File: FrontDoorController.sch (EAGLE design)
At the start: 2 parts

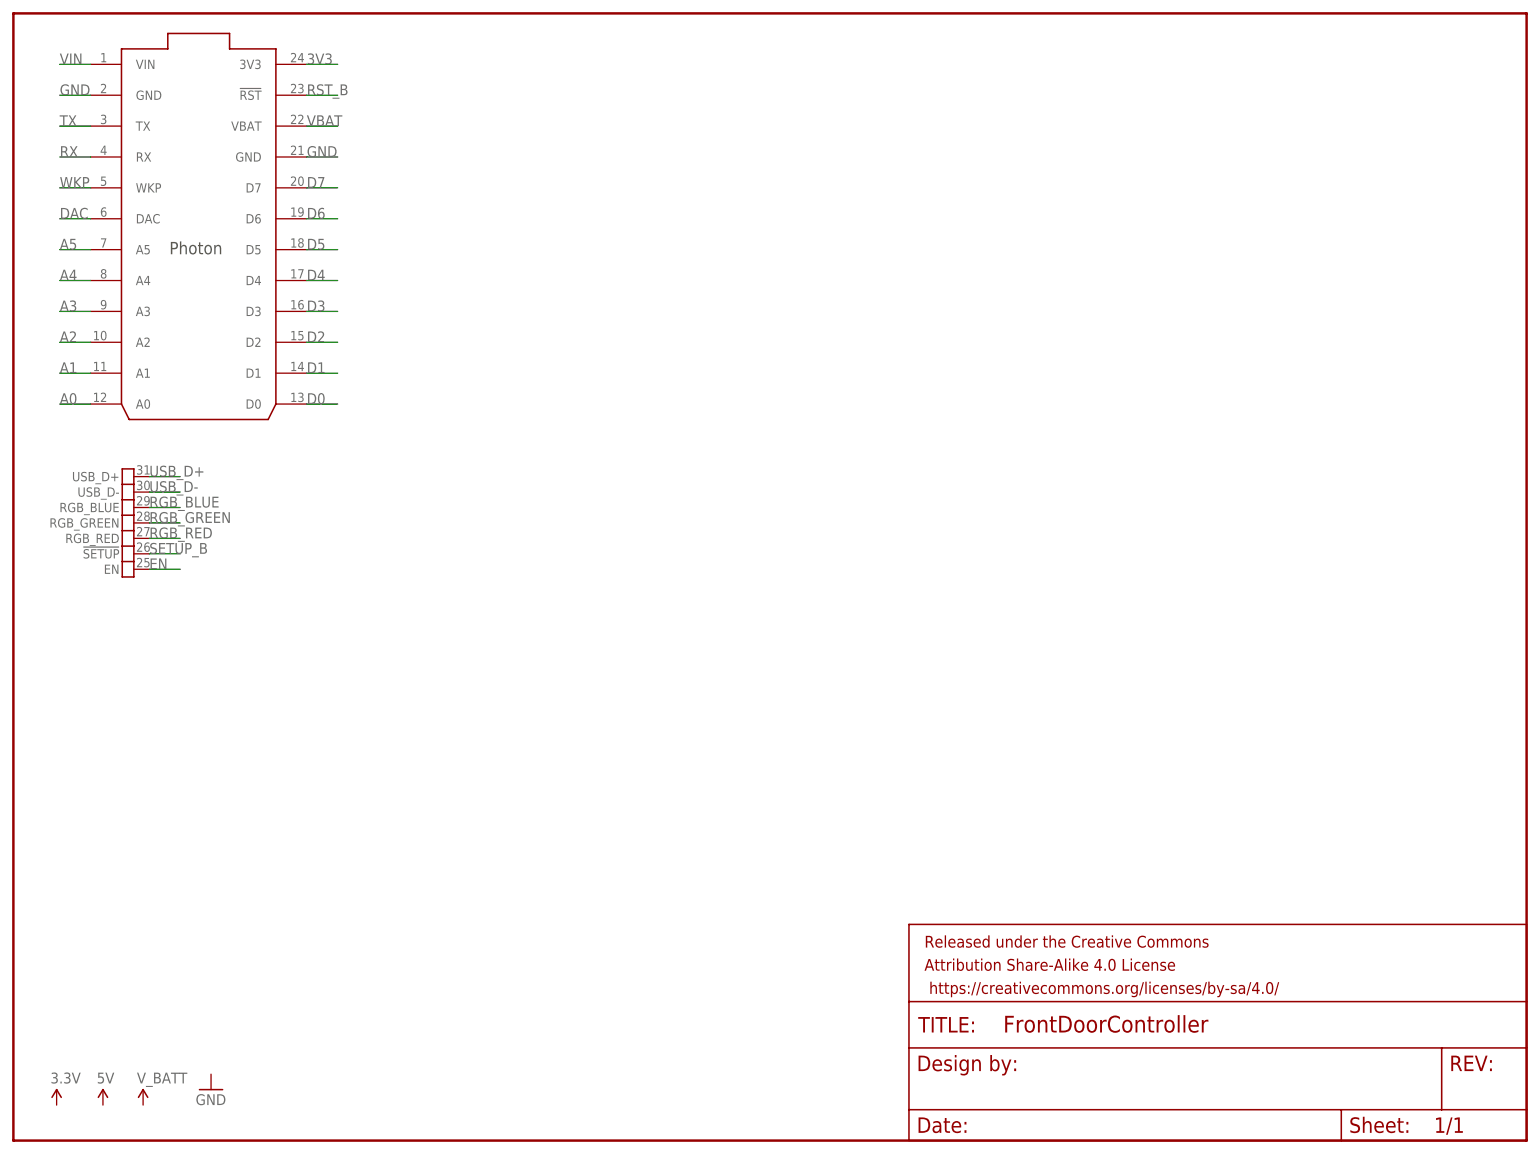
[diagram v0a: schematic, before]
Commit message: Door_Control_PCB: Add motor driver and connect
Add the TB6612FNG motor driver and connect it to the Photon.  This will
take power from 4 AA batteries in the Lockitron and drive the Lockitron
motor.  The Photon will control direction and speed for the motor.
Since there is only 1 motor on the Lockitron, only 1 of the input/output
pairs on the driver needs to be connected.
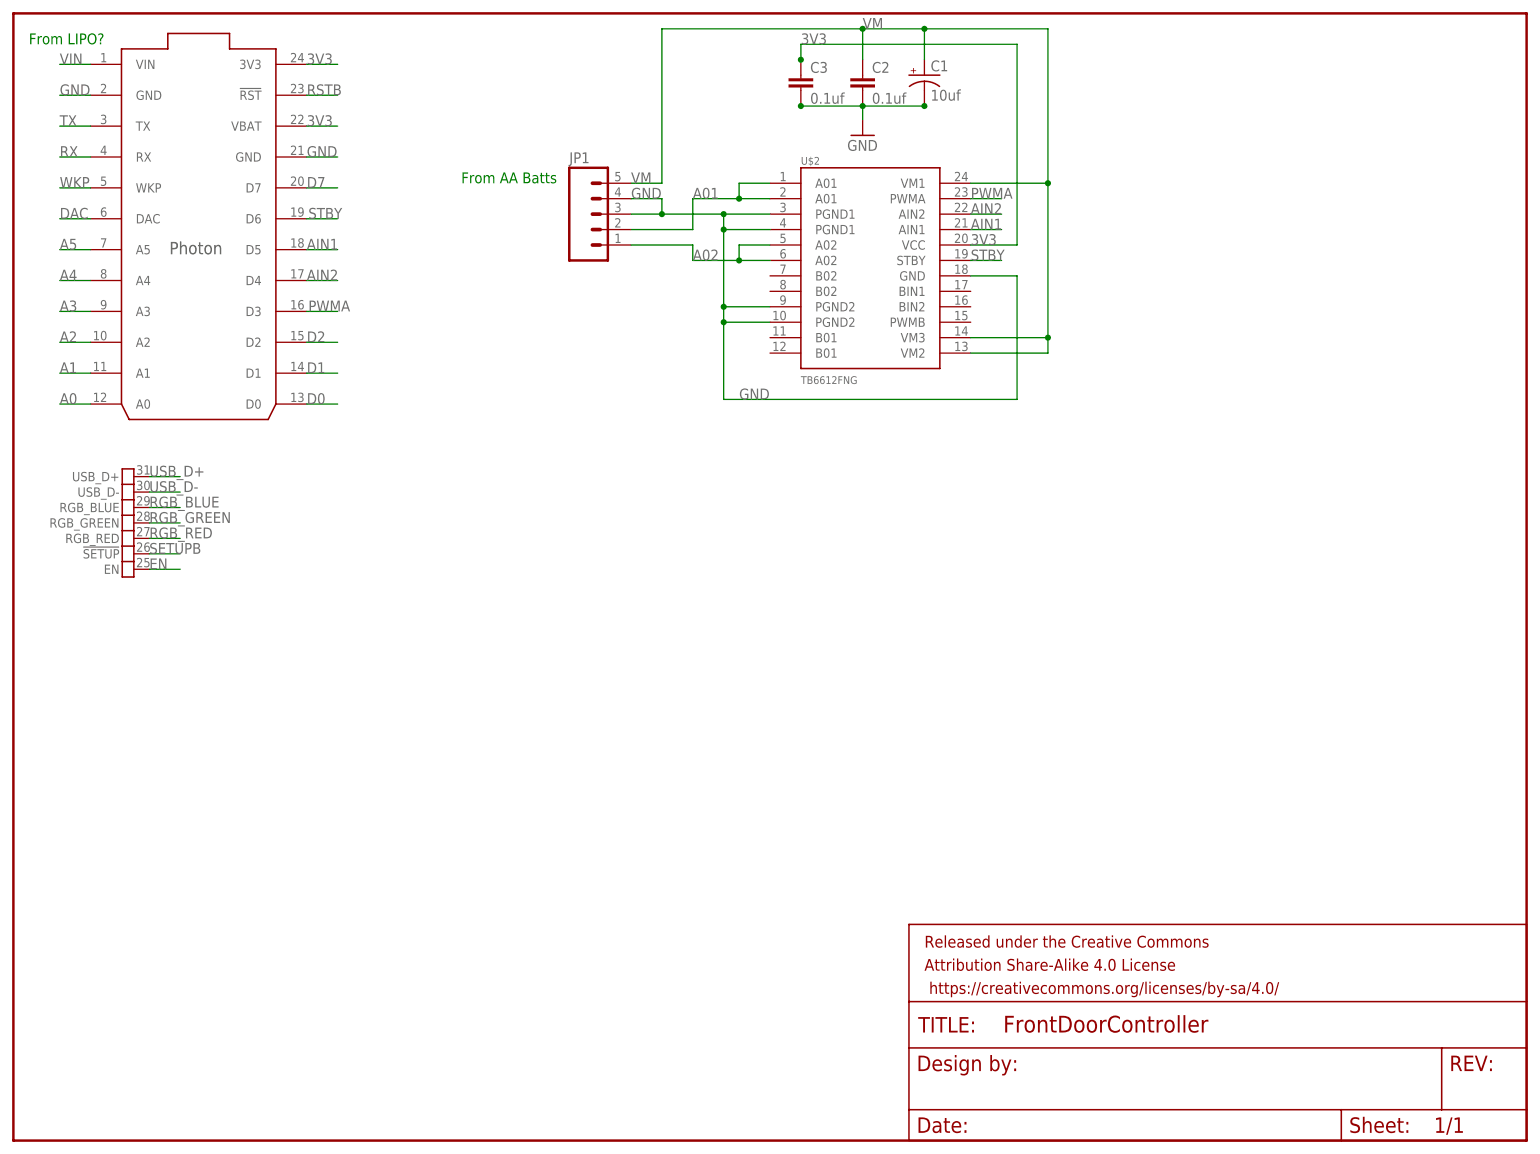
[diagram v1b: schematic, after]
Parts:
- added C1: 10uf, SparkFun-Capacitors:CAP_POL3528
- added C2, C3: 0.1uf, SparkFun-Capacitors:CAP0402-CAP
- added JP1: (no value), SparkFun-Connectors:M05SCREW
- added U$2: TB6612FNG, SparkFun-PowerIC:TB6612FNG
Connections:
- net RST_B renamed RSTB
- net SETUP_B renamed SETUPB
- removed net D3: U$1G$1.D3
- removed net D4: U$1G$1.D4
- removed net D5: U$1G$1.D5
- removed net D6: U$1G$1.D6
- removed net VBAT: U$1G$1.VBAT
- new net A01: JP1.2, U$2.A01@1, U$2.A01@2
- new net A02: JP1.1, U$2.A02@5, U$2.A02@6
- new net AIN1: U$1G$1.D5, U$2.AIN1
- new net AIN2: U$1G$1.D4, U$2.AIN2
- new net PWMA: U$1G$1.D3, U$2.PWMA
- new net STBY: U$1G$1.D6, U$2.STBY
- new net VM: C1.+, C2.1, JP1.5, U$2.VM1, U$2.VM2, U$2.VM3
- net 3V3: now also C3.1, U$1G$1.VBAT, U$2.VCC
- net GND: now also C1.-, C2.2, C3.2, JP1.3, JP1.4, U$2.GND, U$2.PGND1@3, U$2.PGND1@4, U$2.PGND2@10, U$2.PGND2@9
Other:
- note added: "From AA Batts"
- note added: "From LIPO?"

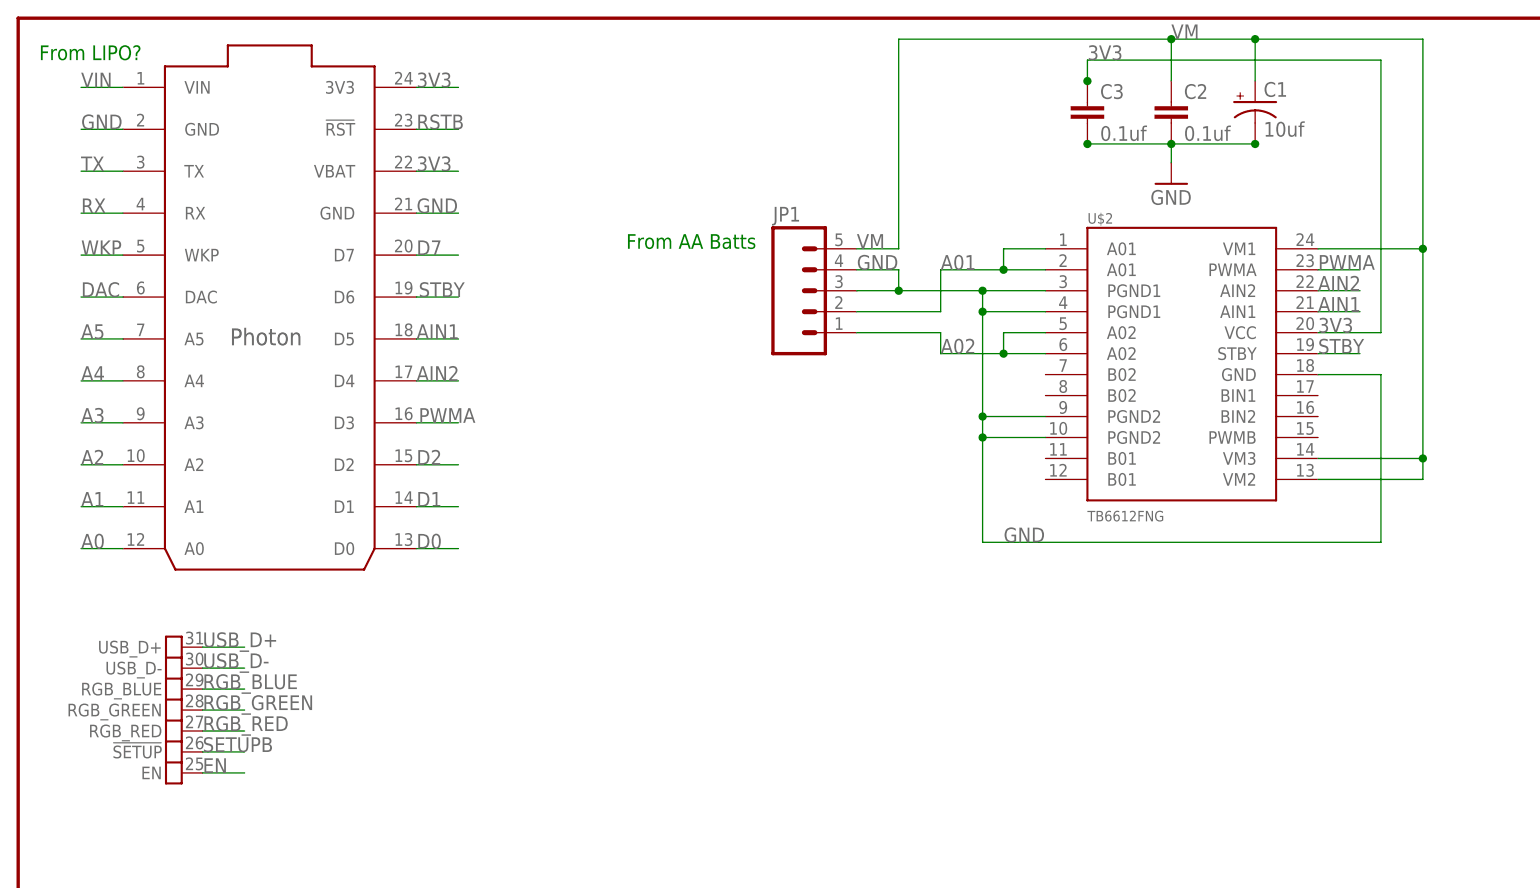
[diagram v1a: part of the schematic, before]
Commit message: Door_Control_PCB: Add headers and diode
Exchange the screw terminals for 0.1" breakaway header holes.  There is
no room for the screw terminals in the Lockitron so wires will need to
be soldered directly to the board.  Some space can be saved by using
0.1" spacing header holes instead of the bigger pitch screw terminals.
Also do a few other minor cleanup tasks like change the size of the wire
input labels.  Also add a 1N4001 diode between VM from AA's and VIN on
Photon to drop the voltage from about 6V to about 5V to ensure it is
safe for the Photon VIN input.
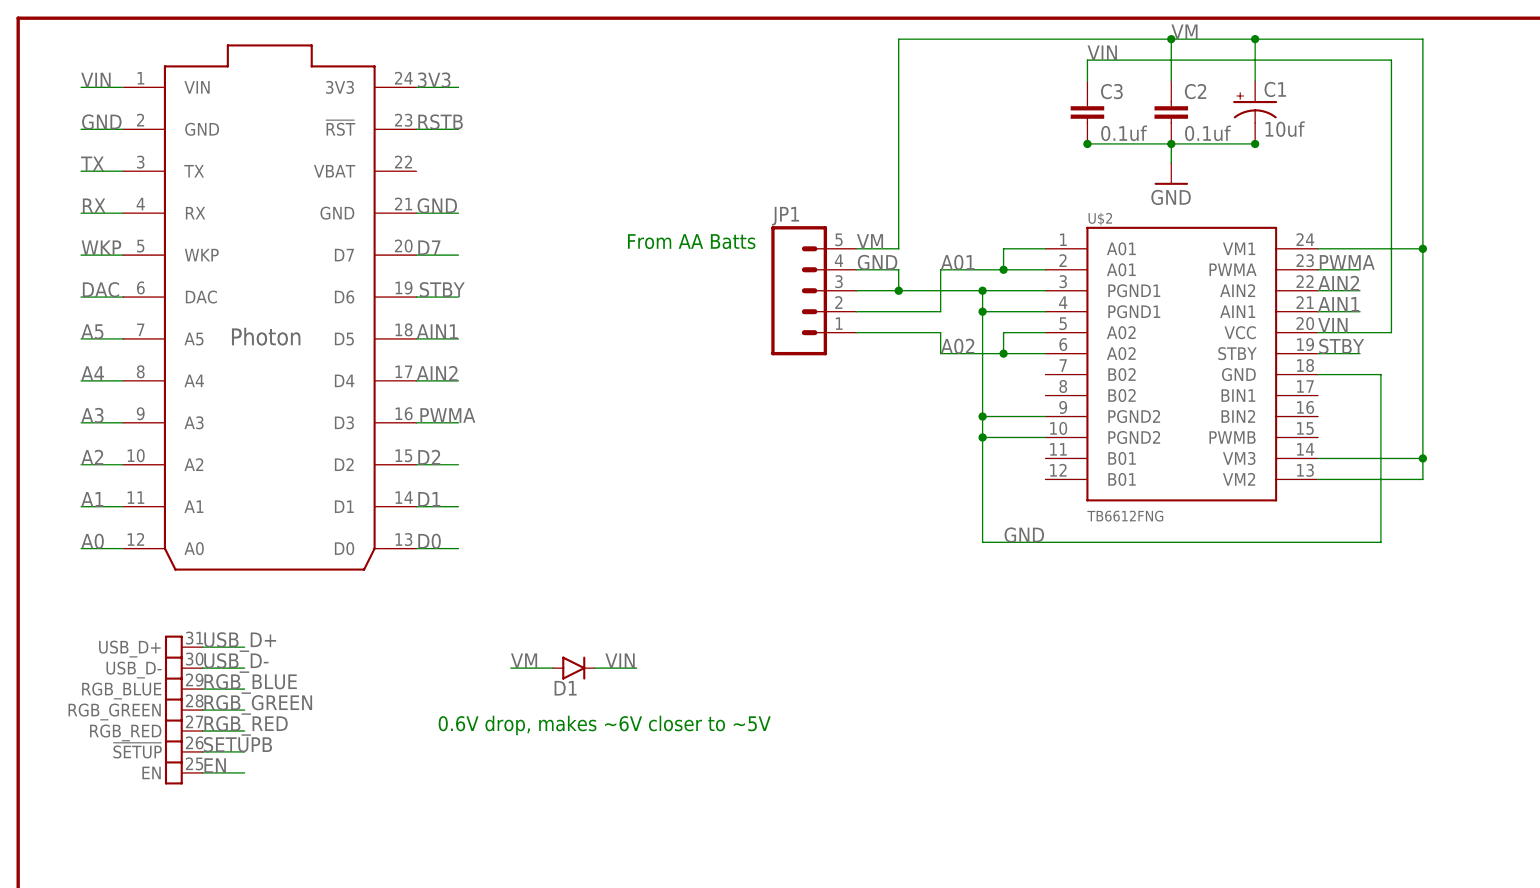
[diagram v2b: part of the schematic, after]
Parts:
- added D1: (no value), SparkFun-DiscreteSemi:DIODEPTH
- JP1: device SparkFun-Connectors:M05SCREW -> SparkFun-Connectors:M05PTH
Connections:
- net 3V3: no longer C3.1, U$1G$1.VBAT, U$2.VCC
- net VIN: now also C3.1, D1.C, U$2.VCC
- net VM: now also D1.A
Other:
- note added: "0.6V drop, makes ~6V closer to ~5V"
- note removed: "From LIPO?"
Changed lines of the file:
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@@
 <part name="C3" library="SparkFun-Capacitors" deviceset="CAP" device="0402-CAP" value="0.1uf"/>
 <part name="GND1" library="SparkFun-Aesthetics" deviceset="GND" device=""/>
-<part name="JP1" library="SparkFun-Connectors" deviceset="M05" device="SCREW"/>
+<part name="JP1" library="SparkFun-Connectors" deviceset="M05" device="PTH"/>
+<part name="D1" library="SparkFun-DiscreteSemi" deviceset="DIODE" device="PTH"/>
 </parts>
 <sheets>
@@
 <plain>
 <text x="73.66" y="157.48" size="1.778" layer="91">From AA Batts</text>
-<text x="2.54" y="180.34" size="1.778" layer="91">From LIPO?</text>
+<text x="50.8" y="99.06" size="1.778" layer="91">0.6V drop, makes ~6V closer to ~5V</text>
 </plain>
 <instances>
@@
 <instance part="GND1" gate="1" x="139.7" y="165.354"/>
 <instance part="JP1" gate="G$1" x="93.98" y="152.4"/>
+<instance part="D1" gate="G$1" x="67.31" y="106.68" smashed="yes">
+<attribute name="NAME" x="64.77" y="103.3526" size="1.778" layer="95"/>
+<attribute name="VALUE" x="69.85" y="104.3686" size="1.778" layer="96"/>
+</instance>
 </instances>
 <busses>
@@
 <wire x1="12.7" y1="177.038" x2="7.62" y2="177.038" width="0.1524" layer="91"/>
 <label x="7.62" y="177.038" size="1.778" layer="95"/>
+</segment>
+<segment>
+<pinref part="D1" gate="G$1" pin="C"/>
+<wire x1="69.85" y1="106.68" x2="74.93" y2="106.68" width="0.1524" layer="91"/>
+<label x="71.12" y="106.68" size="1.778" layer="95"/>
+</segment>
+<segment>
+<pinref part="C3" gate="G$1" pin="1"/>
+<wire x1="129.54" y1="177.8" x2="129.54" y2="180.34" width="0.1524" layer="91"/>
+<wire x1="129.54" y1="180.34" x2="166.37" y2="180.34" width="0.1524" layer="91"/>
+<wire x1="166.37" y1="180.34" x2="166.37" y2="147.32" width="0.1524" layer="91"/>
+<pinref part="U$2" gate="G$1" pin="VCC"/>
+<wire x1="166.37" y1="147.32" x2="157.48" y2="147.32" width="0.1524" layer="91"/>
+<label x="157.48" y="147.32" size="1.778" layer="95"/>
+<label x="129.54" y="180.34" size="1.778" layer="95"/>
 </segment>
 </net>
@@
 <label x="48.26" y="177.038" size="1.778" layer="95"/>
 </segment>
-<segment>
-<pinref part="U$2" gate="G$1" pin="VCC"/>
-<wire x1="157.48" y1="147.32" x2="165.1" y2="147.32" width="0.1524" layer="91"/>
-<label x="157.48" y="147.32" size="1.778" layer="95"/>
-<wire x1="165.1" y1="147.32" x2="165.1" y2="180.34" width="0.1524" layer="91"/>
-<pinref part="C3" gate="G$1" pin="1"/>
-<wire x1="165.1" y1="180.34" x2="129.54" y2="180.34" width="0.1524" layer="91"/>
-<wire x1="129.54" y1="180.34" x2="129.54" y2="177.8" width="0.1524" layer="91"/>
-<label x="129.54" y="180.34" size="1.778" layer="95"/>
-<junction x="129.54" y="177.8"/>
-</segment>
-<segment>
-<pinref part="U$1" gate="G$1" pin="VBAT"/>
-<wire x1="48.26" y1="166.878" x2="53.34" y2="166.878" width="0.1524" layer="91"/>
-<label x="48.26" y="166.878" size="1.778" layer="95"/>
-</segment>
 </net>
 <net name="RSTB" class="0">
@@
 <junction x="139.7" y="182.88"/>
 </segment>
-</net>
+<segment>
+<pinref part="D1" gate="G$1" pin="A"/>
+<wire x1="64.77" y1="106.68" x2="59.69" y2="106.68" width="0.1524" layer="91"/>
+<label x="59.69" y="106.68" size="1.778" layer="95"/>
+</segment>
+</net>
